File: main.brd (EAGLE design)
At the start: 62.4 x 27.5 mm, 16 parts, among them IC1 4558N, J1 DCJ0202, X1 JACK3.5MM

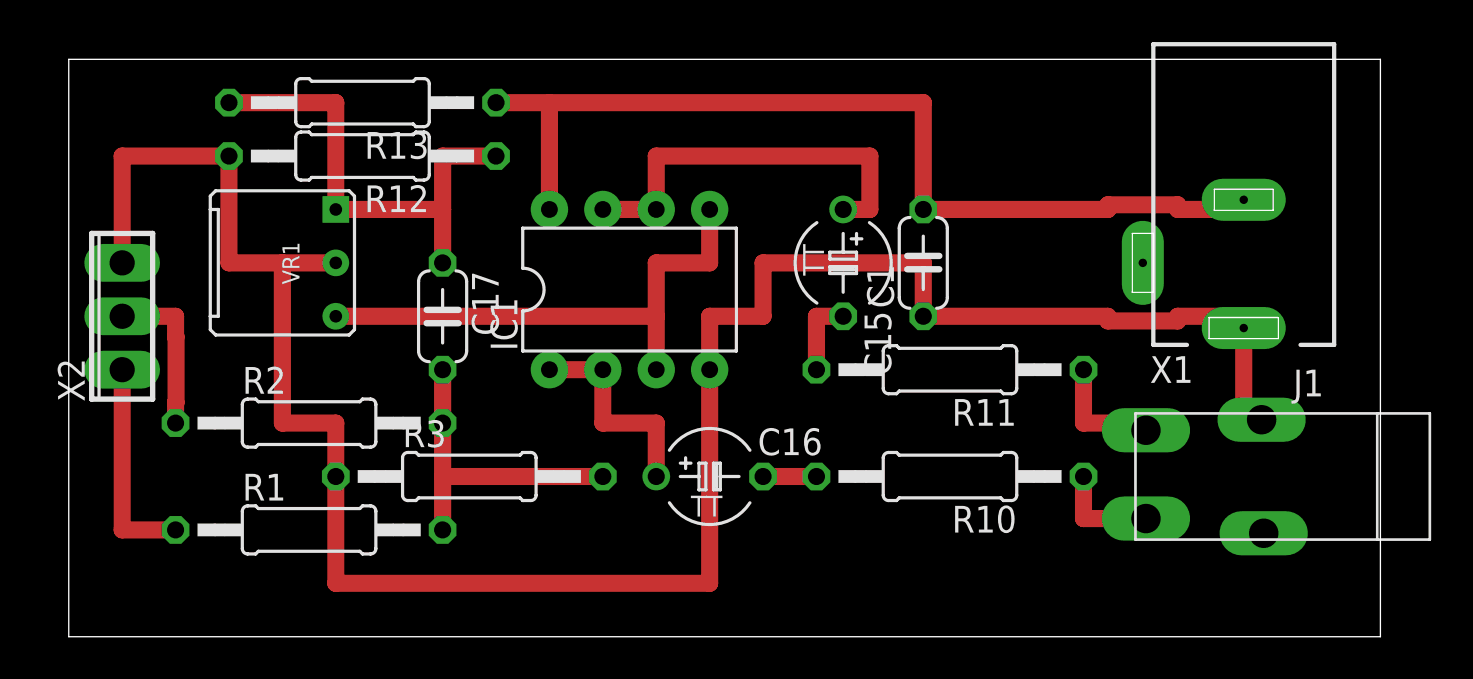
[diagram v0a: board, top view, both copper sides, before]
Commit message: Fix of annotation comment
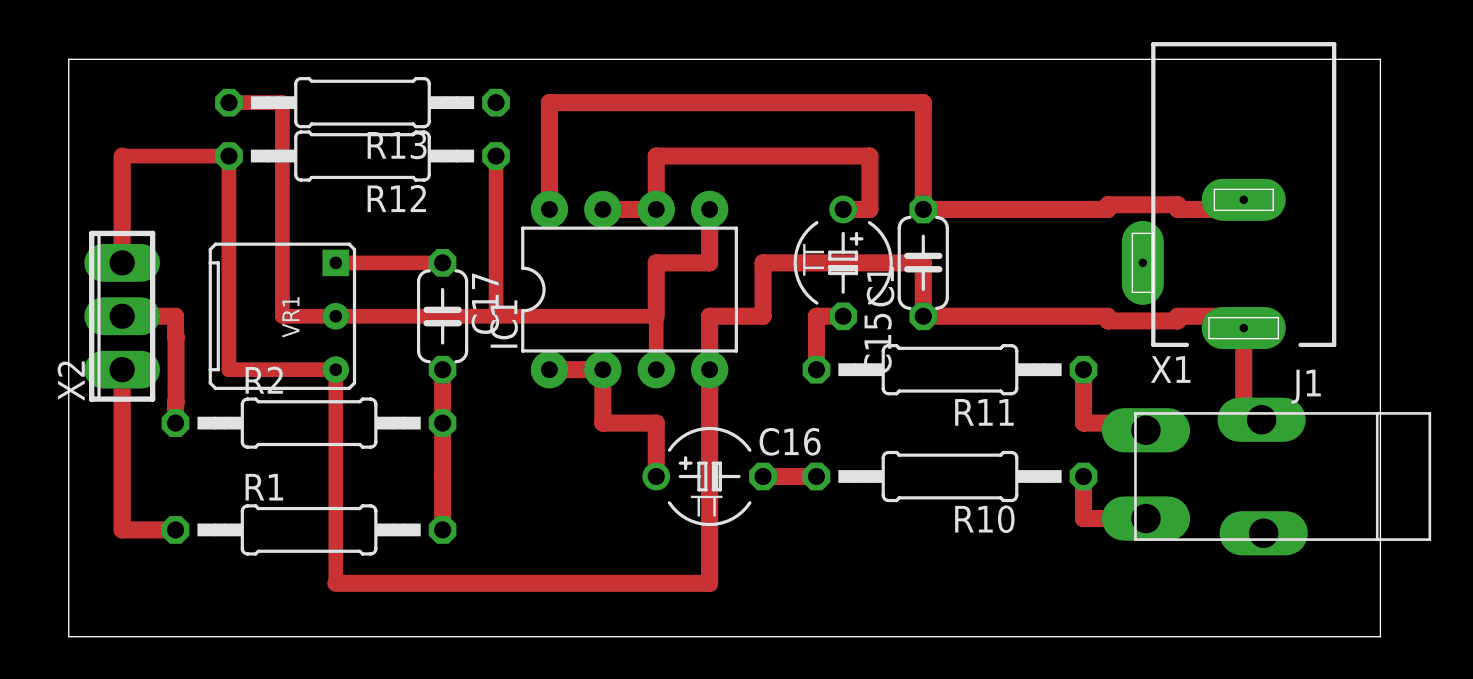
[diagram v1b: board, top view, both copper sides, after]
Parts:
- removed R3: 100K, Resistor:0207(1/4W)
- C1: value 10u -> 0.1u
- moved VR1 2.54 mm to (10.2, 15.2)
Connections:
- removed net N$17: C17.1, R12.1, R13.2, VR1.A
- new net N$6: C17.1, VR1.A
- net GND: now also VR1.E; no longer R3.1, VR1.S
- net N$23: now also R12.1, R13.2, VR1.S; no longer VR1.E
- net N$5: no longer R3.2
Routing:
- net N$23: track 25.4 -> 48.3 mm
- net N$17: track 22.9 -> 0.00 mm
- net N$5: track 15.2 -> 7.62 mm
- net N$6: track 0.00 -> 5.08 mm
- net VCC: track 46.6 -> 44.1 mm
- net GND: track 105.3 -> 102.7 mm
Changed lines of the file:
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@@
 </autorouter>
 <elements>
-<element name="C1" library="Capasitor" package="C050-024X044" value="10u" x="40.64" y="17.78" rot="R90"/>
+<element name="C1" library="Capasitor" package="C050-024X044" value="0.1u" x="40.64" y="17.78" rot="R90"/>
 <element name="C15" library="Capasitor" package="TAP5-45" value="100u6.3" x="36.83" y="17.78" rot="R270"/>
 <element name="C16" library="Capasitor" package="TAP5-45" value="100u6.3" x="30.48" y="7.62"/>
@@
 <element name="R13" library="Resistor" package="0207(1/4W)" value="100K" x="13.97" y="25.4" rot="R180"/>
 <element name="R2" library="Resistor" package="0207(1/4W)" value="33K" x="11.43" y="10.16"/>
-<element name="R3" library="Resistor" package="0207(1/4W)" value="100K" x="19.05" y="7.62"/>
 <element name="X1" library="jack" package="MJ-8435" value="JACK3.5MM" x="62.23" y="7.62" rot="R270"/>
 <element name="X2" library="con-phoenix-254" package="3POL254" value="" x="2.54" y="15.24" rot="R90">
@@
 <attribute name="OC_NEWARK" value="unknown" x="2.54" y="15.24" size="1.778" layer="27" rot="R90" display="off"/>
 </element>
-<element name="VR1" library="Kit" package="POT-ST" value="" x="10.16" y="17.78" rot="R270"/>
+<element name="VR1" library="Kit" package="POT-ST" value="" x="10.16" y="15.24" rot="R270"/>
 </elements>
 <signals>
 <signal name="GND">
-<contactref element="R12" pad="2"/>
 <contactref element="IC1" pad="4"/>
 <contactref element="C1" pad="1"/>
@@
 <contactref element="J1" pad="1"/>
 <contactref element="X2" pad="3"/>
-<contactref element="R3" pad="1"/>
-<contactref element="VR1" pad="S"/>
-<wire x1="7.62" y1="22.86" x2="2.54" y2="22.86" width="0.8128" layer="1"/>
 <wire x1="2.54" y1="22.86" x2="2.54" y2="17.78" width="0.8128" layer="1"/>
-<wire x1="7.62" y1="22.86" x2="7.62" y2="17.78" width="0.8128" layer="1"/>
-<wire x1="7.62" y1="17.78" x2="10.16" y2="17.78" width="0.8128" layer="1"/>
-<wire x1="10.16" y1="17.78" x2="12.7" y2="17.78" width="0.8128" layer="1"/>
 <wire x1="40.64" y1="15.24" x2="40.64" y2="17.78" width="0.8128" layer="1"/>
 <wire x1="40.64" y1="17.78" x2="33.02" y2="17.78" width="0.8128" layer="1"/>
@@
 <wire x1="33.02" y1="15.24" x2="30.48" y2="15.24" width="0.8128" layer="1"/>
 <wire x1="30.48" y1="15.24" x2="30.48" y2="12.7" width="0.8128" layer="1"/>
-<wire x1="12.7" y1="7.62" x2="12.7" y2="10.16" width="0.8128" layer="1"/>
-<wire x1="12.7" y1="10.16" x2="10.16" y2="10.16" width="0.8128" layer="1"/>
-<wire x1="10.16" y1="10.16" x2="10.16" y2="17.78" width="0.8128" layer="1"/>
-<wire x1="12.7" y1="7.62" x2="12.7" y2="2.54" width="0.8128" layer="1"/>
 <wire x1="12.7" y1="2.54" x2="30.48" y2="2.54" width="0.8128" layer="1"/>
 <wire x1="30.48" y1="2.54" x2="30.48" y2="12.7" width="0.8128" layer="1"/>
@@
 <wire x1="56.73" y1="10.32" x2="55.88" y2="10.32" width="0.8128" layer="1"/>
 <wire x1="55.88" y1="10.32" x2="55.88" y2="14.68" width="0.8128" layer="1"/>
+<contactref element="VR1" pad="E"/>
+<contactref element="R12" pad="2"/>
+<wire x1="12.7" y1="12.7" x2="7.62" y2="12.7" width="0.7" layer="1"/>
+<wire x1="7.62" y1="12.7" x2="7.62" y2="22.86" width="0.7" layer="1"/>
+<wire x1="7.62" y1="22.86" x2="2.54" y2="22.86" width="0.7" layer="1"/>
+<wire x1="12.7" y1="12.7" x2="12.7" y2="2.54" width="0.7" layer="1"/>
 </signal>
 <signal name="VCC">
-<contactref element="R13" pad="1"/>
 <contactref element="IC1" pad="8"/>
 <contactref element="C1" pad="2"/>
 <contactref element="J1" pad="3"/>
-<wire x1="20.32" y1="25.4" x2="22.86" y2="25.4" width="0.8128" layer="1"/>
 <wire x1="22.86" y1="25.4" x2="22.86" y2="20.32" width="0.8128" layer="1"/>
 <wire x1="22.86" y1="25.4" x2="40.64" y2="25.4" width="0.8128" layer="1"/>
@@
 <wire x1="52.7404" y1="20.542" x2="52.7404" y2="20.32" width="0.8128" layer="1"/>
 <wire x1="52.7404" y1="20.32" x2="55.88" y2="20.32" width="0.8128" layer="1"/>
+<contactref element="R13" pad="1"/>
+<wire x1="22.86" y1="25.4" x2="20.32" y2="25.4" width="0" layer="19" extent="1-1"/>
 </signal>
-<signal name="N$17">
-<contactref element="C17" pad="1"/>
+<signal name="N$23">
+<contactref element="IC1" pad="5"/>
+<wire x1="30.48" y1="20.32" x2="30.48" y2="17.78" width="0.8128" layer="1"/>
+<wire x1="30.48" y1="17.78" x2="27.94" y2="17.78" width="0.8128" layer="1"/>
+<wire x1="27.94" y1="15.24" x2="27.94" y2="17.78" width="0.8128" layer="1"/>
+<contactref element="IC1" pad="3"/>
+<contactref element="VR1" pad="S"/>
 <contactref element="R13" pad="2"/>
 <contactref element="R12" pad="1"/>
-<contactref element="VR1" pad="A"/>
-<wire x1="7.62" y1="25.4" x2="12.7" y2="25.4" width="0.8128" layer="1"/>
-<wire x1="12.7" y1="25.4" x2="12.7" y2="20.32" width="0.8128" layer="1"/>
-<wire x1="12.7" y1="20.32" x2="17.78" y2="20.32" width="0.8128" layer="1"/>
-<wire x1="17.78" y1="20.32" x2="17.78" y2="17.78" width="0.8128" layer="1"/>
-<wire x1="20.32" y1="22.86" x2="17.78" y2="22.86" width="0.8128" layer="1"/>
-<wire x1="17.78" y1="22.86" x2="17.78" y2="20.32" width="0.8128" layer="1"/>
-</signal>
-<signal name="N$23">
-<contactref element="IC1" pad="3"/>
-<contactref element="IC1" pad="5"/>
-<contactref element="VR1" pad="E"/>
-<wire x1="30.48" y1="20.32" x2="30.48" y2="17.78" width="0.8128" layer="1"/>
-<wire x1="30.48" y1="17.78" x2="27.94" y2="17.78" width="0.8128" layer="1"/>
-<wire x1="27.94" y1="17.78" x2="27.94" y2="15.24" width="0.8128" layer="1"/>
-<wire x1="27.94" y1="15.24" x2="27.94" y2="12.7" width="0.8128" layer="1"/>
-<wire x1="12.7" y1="15.24" x2="27.94" y2="15.24" width="0.8128" layer="1"/>
+<wire x1="12.7" y1="15.24" x2="20.32" y2="15.24" width="0.7" layer="1"/>
+<wire x1="20.32" y1="15.24" x2="20.32" y2="22.86" width="0.7" layer="1"/>
+<wire x1="20.32" y1="15.24" x2="27.94" y2="15.24" width="0.7" layer="1"/>
+<wire x1="27.94" y1="15.24" x2="27.94" y2="12.7" width="0.7" layer="1"/>
+<wire x1="12.7" y1="15.24" x2="10.16" y2="15.24" width="0.7" layer="1"/>
+<wire x1="10.16" y1="15.24" x2="10.16" y2="25.4" width="0.7" layer="1"/>
+<wire x1="10.16" y1="25.4" x2="7.62" y2="25.4" width="0.7" layer="1"/>
 </signal>
 <signal name="N$24">
@@
 <contactref element="R2" pad="2"/>
 <contactref element="C17" pad="2"/>
-<contactref element="R3" pad="2"/>
 <wire x1="17.78" y1="10.16" x2="17.78" y2="7.62" width="0.8128" layer="1"/>
 <wire x1="17.78" y1="7.62" x2="17.78" y2="5.08" width="0.8128" layer="1"/>
-<wire x1="17.78" y1="7.62" x2="25.4" y2="7.62" width="0.8128" layer="1"/>
 <wire x1="17.78" y1="10.16" x2="17.78" y2="12.7" width="0.8128" layer="1"/>
 </signal>
+<signal name="N$6">
+<contactref element="C17" pad="1"/>
+<contactref element="VR1" pad="A"/>
+<wire x1="12.7" y1="17.78" x2="17.78" y2="17.78" width="0.7" layer="1"/>
+</signal>
 </signals>

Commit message: fix
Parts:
- R1, R2: value 33K -> 100R
- R10, R11: value 15K -> 100R
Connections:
- net GND: now also J1.3; no longer J1.1
- net VCC: now also J1.1; no longer J1.3
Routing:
- net GND: track 102.7 -> 97.8 mm
- net VCC: track 44.1 -> 46.2 mm
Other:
- board size 62.4 x 27.5 mm -> 63.7 x 27.5 mm
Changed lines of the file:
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@@
 <setting verticaltext="up"/>
 </settings>
-<grid distance="2.54" unitdist="mm" unit="mm" style="dots" multiple="1" display="yes" altdistance="1.27" altunitdist="mm" altunit="mm"/>
+<grid distance="2.54" unitdist="mm" unit="mm" style="lines" multiple="1" display="yes" altdistance="1.27" altunitdist="mm" altunit="mm"/>
 <layers>
 <layer number="1" name="Top" color="4" fill="1" visible="yes" active="yes"/>
@@
 <board>
 <plain>
-<wire x1="0" y1="0" x2="62.38" y2="0" width="0" layer="20"/>
+<wire x1="-1.27" y1="0" x2="62.38" y2="0" width="0" layer="20"/>
 <wire x1="62.38" y1="0" x2="62.38" y2="27.46" width="0" layer="20"/>
-<wire x1="62.38" y1="27.46" x2="0" y2="27.46" width="0" layer="20"/>
-<wire x1="0" y1="27.46" x2="0" y2="0" width="0" layer="20"/>
+<wire x1="62.38" y1="27.46" x2="-1.27" y2="27.46" width="0" layer="20"/>
+<wire x1="-1.27" y1="27.46" x2="-1.27" y2="0" width="0" layer="20"/>
 </plain>
 <attributes>
@@
 <element name="IC1" library="OPAMP" package="DIP08" value="4558N" x="26.67" y="16.51" rot="R90"/>
 <element name="J1" library="jack" package="DCJ0202" value="DCJ0202" x="55.88" y="17.78" rot="R180"/>
-<element name="R1" library="Resistor" package="0207(1/4W)" value="33K" x="11.43" y="5.08"/>
-<element name="R10" library="Resistor" package="0207(1/4W)" value="15K" x="41.91" y="7.62" rot="R180"/>
-<element name="R11" library="Resistor" package="0207(1/4W)" value="15K" x="41.91" y="12.7" rot="R180"/>
+<element name="R1" library="Resistor" package="0207(1/4W)" value="100R" x="11.43" y="5.08"/>
+<element name="R10" library="Resistor" package="0207(1/4W)" value="100R" x="41.91" y="7.62" rot="R180"/>
+<element name="R11" library="Resistor" package="0207(1/4W)" value="100R" x="41.91" y="12.7" rot="R180"/>
 <element name="R12" library="Resistor" package="0207(1/4W)" value="100K" x="13.97" y="22.86" rot="R180"/>
 <element name="R13" library="Resistor" package="0207(1/4W)" value="100K" x="13.97" y="25.4" rot="R180"/>
-<element name="R2" library="Resistor" package="0207(1/4W)" value="33K" x="11.43" y="10.16"/>
+<element name="R2" library="Resistor" package="0207(1/4W)" value="100R" x="11.43" y="10.16"/>
 <element name="X1" library="jack" package="MJ-8435" value="JACK3.5MM" x="62.23" y="7.62" rot="R270"/>
 <element name="X2" library="con-phoenix-254" package="3POL254" value="" x="2.54" y="15.24" rot="R90">
@@
 <contactref element="C1" pad="1"/>
 <contactref element="X1" pad="2@1"/>
-<contactref element="J1" pad="1"/>
 <contactref element="X2" pad="3"/>
 <wire x1="2.54" y1="22.86" x2="2.54" y2="17.78" width="0.8128" layer="1"/>
@@
 <wire x1="12.7" y1="2.54" x2="30.48" y2="2.54" width="0.8128" layer="1"/>
 <wire x1="30.48" y1="2.54" x2="30.48" y2="12.7" width="0.8128" layer="1"/>
-<wire x1="55.88" y1="15.24" x2="55.88" y2="14.68" width="0.8128" layer="1"/>
 <wire x1="40.64" y1="15.24" x2="49.4196" y2="15.24" width="0.8128" layer="1"/>
 <wire x1="49.4196" y1="15.24" x2="49.4196" y2="15.018" width="0.8128" layer="1"/>
@@
 <wire x1="52.7404" y1="15.24" x2="55.88" y2="15.24" width="0.8128" layer="1"/>
 <wire x1="56.73" y1="10.32" x2="55.88" y2="10.32" width="0.8128" layer="1"/>
-<wire x1="55.88" y1="10.32" x2="55.88" y2="14.68" width="0.8128" layer="1"/>
 <contactref element="VR1" pad="E"/>
 <contactref element="R12" pad="2"/>
@@
 <wire x1="7.62" y1="22.86" x2="2.54" y2="22.86" width="0.7" layer="1"/>
 <wire x1="12.7" y1="12.7" x2="12.7" y2="2.54" width="0.7" layer="1"/>
+<contactref element="J1" pad="3"/>
+<wire x1="55.88" y1="15.24" x2="55.88" y2="20.78" width="0" layer="19" extent="1-1"/>
+<wire x1="55.88" y1="10.32" x2="55.88" y2="15.24" width="0" layer="19" extent="1-1"/>
 </signal>
 <signal name="VCC">
 <contactref element="IC1" pad="8"/>
 <contactref element="C1" pad="2"/>
-<contactref element="J1" pad="3"/>
 <wire x1="22.86" y1="25.4" x2="22.86" y2="20.32" width="0.8128" layer="1"/>
 <wire x1="22.86" y1="25.4" x2="40.64" y2="25.4" width="0.8128" layer="1"/>
 <wire x1="40.64" y1="25.4" x2="40.64" y2="20.32" width="0.8128" layer="1"/>
-<wire x1="55.88" y1="20.32" x2="55.88" y2="20.78" width="0.8128" layer="1"/>
 <wire x1="40.64" y1="20.32" x2="49.4196" y2="20.32" width="0.8128" layer="1"/>
 <wire x1="49.4196" y1="20.32" x2="49.4196" y2="20.542" width="0.8128" layer="1"/>
@@
 <wire x1="52.7404" y1="20.32" x2="55.88" y2="20.32" width="0.8128" layer="1"/>
 <contactref element="R13" pad="1"/>
-<wire x1="22.86" y1="25.4" x2="20.32" y2="25.4" width="0" layer="19" extent="1-1"/>
+<wire x1="20.32" y1="25.4" x2="22.86" y2="25.4" width="0.7" layer="1"/>
+<contactref element="J1" pad="1"/>
+<wire x1="55.88" y1="20.32" x2="55.88" y2="14.68" width="0" layer="19" extent="1-1"/>
 </signal>
 <signal name="N$23">
